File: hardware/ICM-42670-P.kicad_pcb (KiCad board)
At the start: 2 copper layers, 22.5 x 15.8 mm, 7 parts, among them J1 Connector

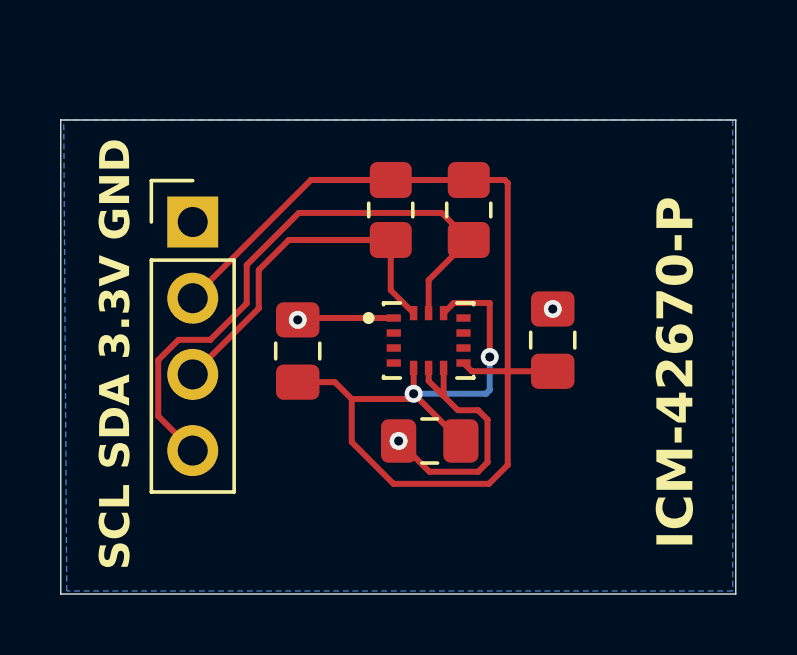
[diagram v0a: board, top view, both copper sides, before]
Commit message: fix vias
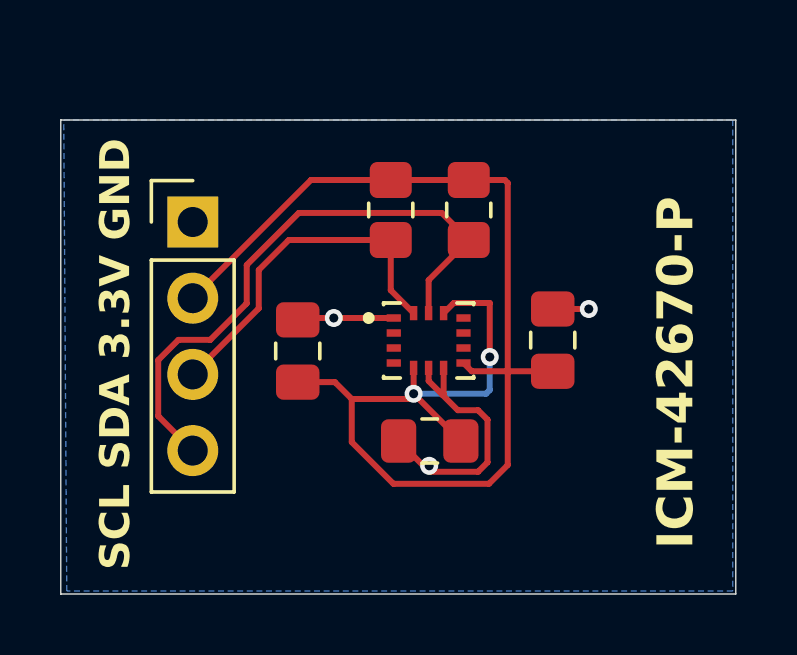
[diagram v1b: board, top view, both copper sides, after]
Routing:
- net GND: track 12.0 -> 13.3 mm
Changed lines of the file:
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@@
 	)
 	(segment
-		(start 145.8885 95.626)
-		(end 144.8625 94.6)
+		(start 147.51016 93.574)
+		(end 146.8365 93.574)
+		(width 0.2)
+		(layer "F.Cu")
+		(net 2)
+	)
+	(segment
+		(start 142.7 90.5)
+		(end 144.7 90.5)
+		(width 0.2)
+		(layer "F.Cu")
+		(net 2)
+	)
+	(segment
+		(start 146.8365 93.574)
+		(end 146.33125 93.06875)
 		(width 0.2)
 		(layer "F.Cu")
@@
 	(segment
 		(start 147.826 95.31016)
+		(end 147.826 93.88984)
+		(width 0.2)
+		(layer "F.Cu")
+		(net 2)
+	)
+	(segment
+		(start 145.8885 95.626)
 		(end 147.51016 95.626)
+		(width 0.2)
+		(layer "F.Cu")
+		(net 2)
+	)
+	(segment
+		(start 151.2 90.2)
+		(end 150 90.2)
+		(width 0.2)
+		(layer "F.Cu")
+		(net 2)
+	)
+	(segment
+		(start 145.6895 95.427)
+		(end 144.8625 94.6)
 		(width 0.2)
 		(layer "F.Cu")
@@
 	(segment
 		(start 147.51016 95.626)
-		(end 145.8885 95.626)
+		(end 147.826 95.31016)
 		(width 0.2)
 		(layer "F.Cu")
@@
 	)
 	(segment
-		(start 146.8365 93.574)
+		(start 142.7 90.5)
+		(end 141.5625 90.5)
+		(width 0.2)
+		(layer "F.Cu")
+		(net 2)
+	)
+	(segment
+		(start 147.826 93.88984)
 		(end 147.51016 93.574)
 		(width 0.2)
@@
 	)
 	(segment
-		(start 147.826 93.88984)
-		(end 147.826 95.31016)
+		(start 145.88125 95.427)
+		(end 145.88125 95.61875)
 		(width 0.2)
 		(layer "F.Cu")
@@
 	)
 	(segment
-		(start 147.51016 93.574)
-		(end 147.826 93.88984)
+		(start 145.88125 95.427)
+		(end 145.6895 95.427)
 		(width 0.2)
 		(layer "F.Cu")
@@
 	)
 	(segment
-		(start 144.7 90.5)
-		(end 141.5625 90.5)
+		(start 141.5625 90.5)
+		(end 141.5 90.5625)
 		(width 0.2)
 		(layer "F.Cu")
@@
 		(start 145.8625 92.6)
 		(end 146.33125 93.06875)
+		(width 0.2)
+		(layer "F.Cu")
+		(net 2)
+	)
+	(segment
+		(start 145.88125 95.61875)
+		(end 145.8885 95.626)
 		(width 0.2)
 		(layer "F.Cu")
@@
 		(net 2)
 	)
-	(segment
-		(start 141.5625 90.5)
-		(end 141.5 90.5625)
-		(width 0.2)
-		(layer "F.Cu")
-		(net 2)
-	)
-	(segment
-		(start 146.33125 93.06875)
-		(end 146.8365 93.574)
-		(width 0.2)
-		(layer "F.Cu")
-		(net 2)
-	)
 	(via
-		(at 150 90.2)
+		(at 151.2 90.2)
 		(size 0.6)
 		(drill 0.3)
@@
 	)
 	(via
-		(at 144.8625 94.6)
+		(at 145.88125 95.427)
 		(size 0.6)
 		(drill 0.3)
@@
 	)
 	(via
-		(at 141.5 90.5625)
+		(at 142.7 90.5)
 		(size 0.6)
 		(drill 0.3)
